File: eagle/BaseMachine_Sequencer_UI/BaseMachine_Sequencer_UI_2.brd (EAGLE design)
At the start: 71.7 x 46.6 mm, 4 parts, among them SW1 AK_TCTSW, SW2 AK_TCTSW

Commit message: Update: UI & UI2 Board Design
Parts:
- added JP2: PWR1, pinhead:1X02/90
- added JP3: PWR2, pinhead:1X02
- added JP4: PWR3, pinhead:1X02
- added JP5: PWR4, pinhead:1X02
- added JP6: PWR5, pinhead:1X02
- added SW3: AK_TCTSW, mylib2:TME1
- JP1: value (none) -> SW1
- moved JP1 15.5 mm to (39.1, 44.5)
- moved SW2 7.71 mm to (53.2, 15.2)
- moved RE1 5.75 mm to (10.2, 17.7)
- moved SW1 2.57 mm to (35.0, 15.6)
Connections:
- removed net N$3: JP1.1, RE1.P$2
- removed net N$6: JP1.4, SW2.3, SW2.4
- new net N$1: JP1.2, RE1.P$2
- new net N$2: JP1.5, SW2.3, SW2.4
- new net N$7: JP1.1, SW3.3, SW3.4
- new net VCC: JP2.1, JP3.1, JP4.1, JP5.1, JP6.1
- net GND: now also JP2.2, JP3.2, JP4.2, JP5.2, JP6.2, SW3.1, SW3.6; no longer JP1.5
- net N$4: now also JP1.3; no longer JP1.2
- net N$5: now also JP1.4; no longer JP1.3
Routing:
- net GND: track 0.00 -> 138.9 mm
- net N$1: track 0.00 -> 54.1 mm
- net N$4: track 0.00 -> 51.6 mm
- net N$2: track 0.00 -> 36.3 mm
- net N$5: track 0.00 -> 33.2 mm
- net N$7: track 0.00 -> 28.9 mm
- net VCC: track 0.00 -> 10.6 mm
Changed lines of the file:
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@@
 </autorouter>
 <elements>
-<element name="RE1" library="mylib2" package="RE_AK_DIP" value="RE_AK_DIP" x="12.73" y="22.86"/>
-<element name="SW1" library="mylib2" package="TME1" value="AK_TCTSW" x="32.44" y="15.6" rot="R90"/>
-<element name="SW2" library="mylib2" package="TME1" value="AK_TCTSW" x="60.96" y="15.24" rot="R90"/>
-<element name="JP1" library="pinhead" package="1X05/90" value="" x="54.55" y="45.72"/>
+<element name="RE1" library="mylib2" package="RE_AK_DIP" value="RE_AK_DIP" x="10.16" y="17.72"/>
+<element name="SW1" library="mylib2" package="TME1" value="AK_TCTSW" x="35.01" y="15.6" rot="R90"/>
+<element name="SW2" library="mylib2" package="TME1" value="AK_TCTSW" x="53.25" y="15.24" rot="R90"/>
+<element name="JP1" library="pinhead" package="1X05/90" value="SW1" x="39.13" y="44.45"/>
+<element name="SW3" library="mylib2" package="TME1" value="AK_TCTSW" x="10.25" y="36.77"/>
+<element name="JP2" library="pinhead" package="1X02/90" value="PWR1" x="63.44" y="44.42"/>
+<element name="JP3" library="pinhead" package="1X02" value="PWR2" x="63.44" y="37.92"/>
+<element name="JP4" library="pinhead" package="1X02" value="PWR3" x="63.44" y="35.29"/>
+<element name="JP5" library="pinhead" package="1X02" value="PWR4" x="63.44" y="32.66"/>
+<element name="JP6" library="pinhead" package="1X02" value="PWR5" x="63.44" y="30.03"/>
 </elements>
 <signals>
@@
 <contactref element="SW2" pad="1"/>
 <contactref element="RE1" pad="P$3"/>
-<contactref element="JP1" pad="5"/>
-<wire x1="57.15" y1="12.7" x2="59.63" y2="41.91" width="0" layer="19" extent="1-1"/>
-<wire x1="64.77" y1="12.7" x2="57.15" y2="12.7" width="0" layer="19" extent="1-1"/>
-<wire x1="36.25" y1="13.06" x2="57.15" y2="12.7" width="0" layer="19" extent="1-1"/>
-<wire x1="28.63" y1="13.06" x2="36.25" y2="13.06" width="0" layer="19" extent="1-1"/>
-<wire x1="12.73" y1="12.7" x2="28.63" y2="13.06" width="0" layer="19" extent="1-1"/>
-</signal>
-<signal name="N$3">
-<contactref element="RE1" pad="P$2"/>
-<contactref element="JP1" pad="1"/>
-<wire x1="10.19" y1="12.7" x2="49.47" y2="41.91" width="0" layer="19" extent="1-1"/>
+<contactref element="SW3" pad="1"/>
+<contactref element="SW3" pad="6"/>
+<contactref element="JP4" pad="2"/>
+<contactref element="JP5" pad="2"/>
+<contactref element="JP3" pad="2"/>
+<contactref element="JP6" pad="2"/>
+<contactref element="JP2" pad="2"/>
+<wire x1="7.71" y1="40.58" x2="7.71" y2="32.96" width="0.4064" layer="1"/>
+<wire x1="31.2" y1="13.06" x2="38.82" y2="13.06" width="0.4064" layer="1"/>
+<wire x1="49.44" y1="12.7" x2="56.54" y2="12.7" width="0.4064" layer="1"/>
+<wire x1="56.54" y1="12.7" x2="56.54" y2="12.85" width="0.4064" layer="1"/>
+<wire x1="56.54" y1="12.85" x2="57.06" y2="12.85" width="0.4064" layer="1"/>
+<wire x1="57.06" y1="12.85" x2="57.06" y2="12.7" width="0.4064" layer="1"/>
+<wire x1="64.71" y1="40.61" x2="64.71" y2="37.92" width="0.4064" layer="16"/>
+<wire x1="64.71" y1="37.92" x2="64.71" y2="35.29" width="0.4064" layer="16"/>
+<wire x1="64.71" y1="35.29" x2="64.71" y2="32.66" width="0.4064" layer="16"/>
+<wire x1="64.71" y1="32.66" x2="64.71" y2="30.03" width="0.4064" layer="16"/>
+<wire x1="64.71" y1="30.03" x2="64.25" y2="30.03" width="0.4064" layer="16"/>
+<wire x1="64.25" y1="30.03" x2="64.25" y2="12.85" width="0.4064" layer="16"/>
+<wire x1="64.25" y1="12.85" x2="57.06" y2="12.85" width="0.4064" layer="16"/>
+<wire x1="57.06" y1="12.85" x2="57.06" y2="12.7" width="0.4064" layer="16"/>
+<wire x1="49.44" y1="12.7" x2="38.82" y2="12.7" width="0.4064" layer="16"/>
+<wire x1="38.82" y1="12.7" x2="38.82" y2="13.06" width="0.4064" layer="16"/>
+<wire x1="31.2" y1="13.06" x2="30.84" y2="13.06" width="0.4064" layer="16"/>
+<wire x1="30.84" y1="13.06" x2="30.84" y2="5.14" width="0.4064" layer="16"/>
+<wire x1="30.84" y1="5.14" x2="10.28" y2="5.14" width="0.4064" layer="16"/>
+<wire x1="10.28" y1="5.14" x2="2.57" y2="5.14" width="0.4064" layer="16"/>
+<wire x1="2.57" y1="5.14" x2="2.57" y2="28.27" width="0.4064" layer="16"/>
+<wire x1="2.57" y1="28.27" x2="3.02" y2="28.27" width="0.4064" layer="16"/>
+<wire x1="3.02" y1="28.27" x2="7.71" y2="32.96" width="0.4064" layer="16"/>
+<wire x1="10.16" y1="7.56" x2="10.16" y2="5.26" width="0.4064" layer="16"/>
+<wire x1="10.16" y1="5.26" x2="10.28" y2="5.14" width="0.4064" layer="16"/>
 </signal>
 <signal name="N$4">
 <contactref element="RE1" pad="P$4"/>
-<contactref element="JP1" pad="2"/>
-<wire x1="15.27" y1="12.7" x2="52.01" y2="41.91" width="0" layer="19" extent="1-1"/>
+<contactref element="JP1" pad="3"/>
+<wire x1="12.7" y1="7.56" x2="12.7" y2="17.84" width="0.4064" layer="16"/>
+<wire x1="12.7" y1="17.84" x2="12.85" y2="17.99" width="0.4064" layer="16"/>
+<wire x1="12.85" y1="17.99" x2="12.85" y2="20.56" width="0.4064" layer="16"/>
+<wire x1="12.85" y1="20.56" x2="25.7" y2="20.56" width="0.4064" layer="16"/>
+<wire x1="25.7" y1="20.56" x2="38.55" y2="33.41" width="0.4064" layer="16"/>
+<wire x1="38.55" y1="33.41" x2="38.55" y2="40.06" width="0.4064" layer="16"/>
+<wire x1="38.55" y1="40.06" x2="39.13" y2="40.64" width="0.4064" layer="16"/>
 </signal>
 <signal name="N$5">
 <contactref element="SW1" pad="4"/>
 <contactref element="SW1" pad="3"/>
-<contactref element="JP1" pad="3"/>
-<wire x1="36.25" y1="18.14" x2="54.55" y2="41.91" width="0" layer="19" extent="1-1"/>
-<wire x1="28.63" y1="18.14" x2="36.25" y2="18.14" width="0" layer="19" extent="1-1"/>
+<contactref element="JP1" pad="4"/>
+<wire x1="31.2" y1="18.14" x2="38.55" y2="18.14" width="0.4064" layer="1"/>
+<wire x1="38.55" y1="18.14" x2="38.55" y2="17.99" width="0.4064" layer="1"/>
+<wire x1="38.55" y1="17.99" x2="38.82" y2="17.99" width="0.4064" layer="1"/>
+<wire x1="38.82" y1="17.99" x2="38.82" y2="18.14" width="0.4064" layer="1"/>
+<wire x1="38.82" y1="18.14" x2="40.97" y2="18.14" width="0.4064" layer="16"/>
+<wire x1="40.97" y1="18.14" x2="41.12" y2="17.99" width="0.4064" layer="16"/>
+<wire x1="41.12" y1="17.99" x2="41.12" y2="40.09" width="0.4064" layer="16"/>
+<wire x1="41.12" y1="40.09" x2="41.67" y2="40.64" width="0.4064" layer="16"/>
 </signal>
-<signal name="N$6">
+<signal name="N$2">
 <contactref element="SW2" pad="4"/>
 <contactref element="SW2" pad="3"/>
-<contactref element="JP1" pad="4"/>
-<wire x1="57.15" y1="17.78" x2="57.09" y2="41.91" width="0" layer="19" extent="1-1"/>
-<wire x1="64.77" y1="17.78" x2="57.15" y2="17.78" width="0" layer="19" extent="1-1"/>
+<contactref element="JP1" pad="5"/>
+<wire x1="49.44" y1="17.78" x2="57.06" y2="17.78" width="0.4064" layer="1"/>
+<wire x1="49.44" y1="17.78" x2="43.9" y2="17.78" width="0.4064" layer="16"/>
+<wire x1="43.9" y1="17.78" x2="43.69" y2="17.99" width="0.4064" layer="16"/>
+<wire x1="43.69" y1="17.99" x2="43.69" y2="40.12" width="0.4064" layer="16"/>
+<wire x1="43.69" y1="40.12" x2="44.21" y2="40.64" width="0.4064" layer="16"/>
+</signal>
+<signal name="N$7">
+<contactref element="SW3" pad="4"/>
+<contactref element="SW3" pad="3"/>
+<contactref element="JP1" pad="1"/>
+<wire x1="12.79" y1="40.58" x2="12.79" y2="32.96" width="0.4064" layer="1"/>
+<wire x1="12.79" y1="40.58" x2="33.99" y2="40.58" width="0.4064" layer="16"/>
+<wire x1="33.99" y1="40.58" x2="34.05" y2="40.64" width="0.4064" layer="16"/>
+</signal>
+<signal name="N$1">
+<contactref element="RE1" pad="P$2"/>
+<contactref element="JP1" pad="2"/>
+<wire x1="7.62" y1="7.56" x2="7.62" y2="23.04" width="0.4064" layer="16"/>
+<wire x1="7.62" y1="23.04" x2="7.71" y2="23.13" width="0.4064" layer="16"/>
+<wire x1="7.71" y1="23.13" x2="23.13" y2="23.13" width="0.4064" layer="16"/>
+<wire x1="23.13" y1="23.13" x2="35.98" y2="35.98" width="0.4064" layer="16"/>
+<wire x1="35.98" y1="35.98" x2="35.98" y2="40.03" width="0.4064" layer="16"/>
+<wire x1="35.98" y1="40.03" x2="36.59" y2="40.64" width="0.4064" layer="16"/>
+</signal>
+<signal name="VCC">
+<contactref element="JP6" pad="1"/>
+<contactref element="JP3" pad="1"/>
+<contactref element="JP5" pad="1"/>
+<contactref element="JP4" pad="1"/>
+<contactref element="JP2" pad="1"/>
+<wire x1="62.17" y1="40.61" x2="62.17" y2="37.92" width="0.4064" layer="16"/>
+<wire x1="62.17" y1="37.92" x2="62.17" y2="35.29" width="0.4064" layer="16"/>
+<wire x1="62.17" y1="35.29" x2="62.17" y2="32.66" width="0.4064" layer="16"/>
+<wire x1="62.17" y1="32.66" x2="62.17" y2="30.03" width="0.4064" layer="16"/>
 </signal>
 </signals>

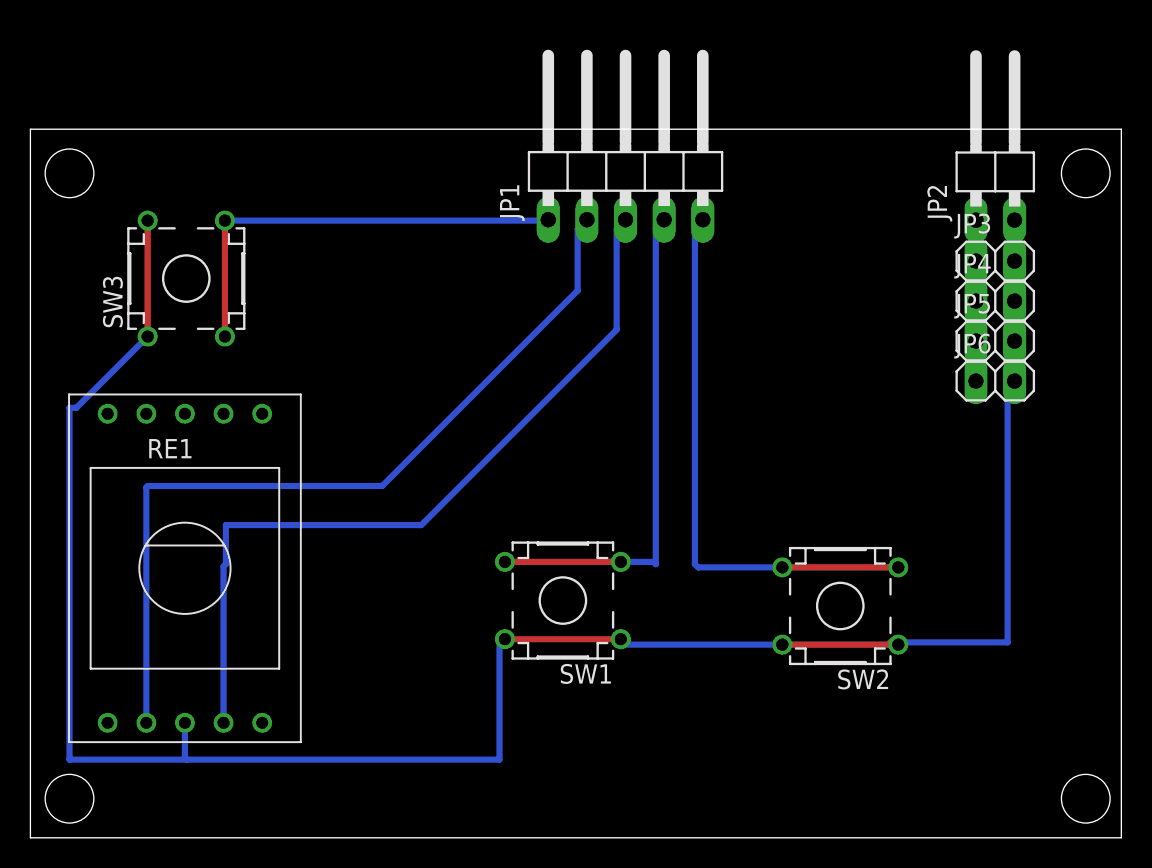
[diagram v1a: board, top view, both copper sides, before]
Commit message: Add: Nucleo firmware's binaries
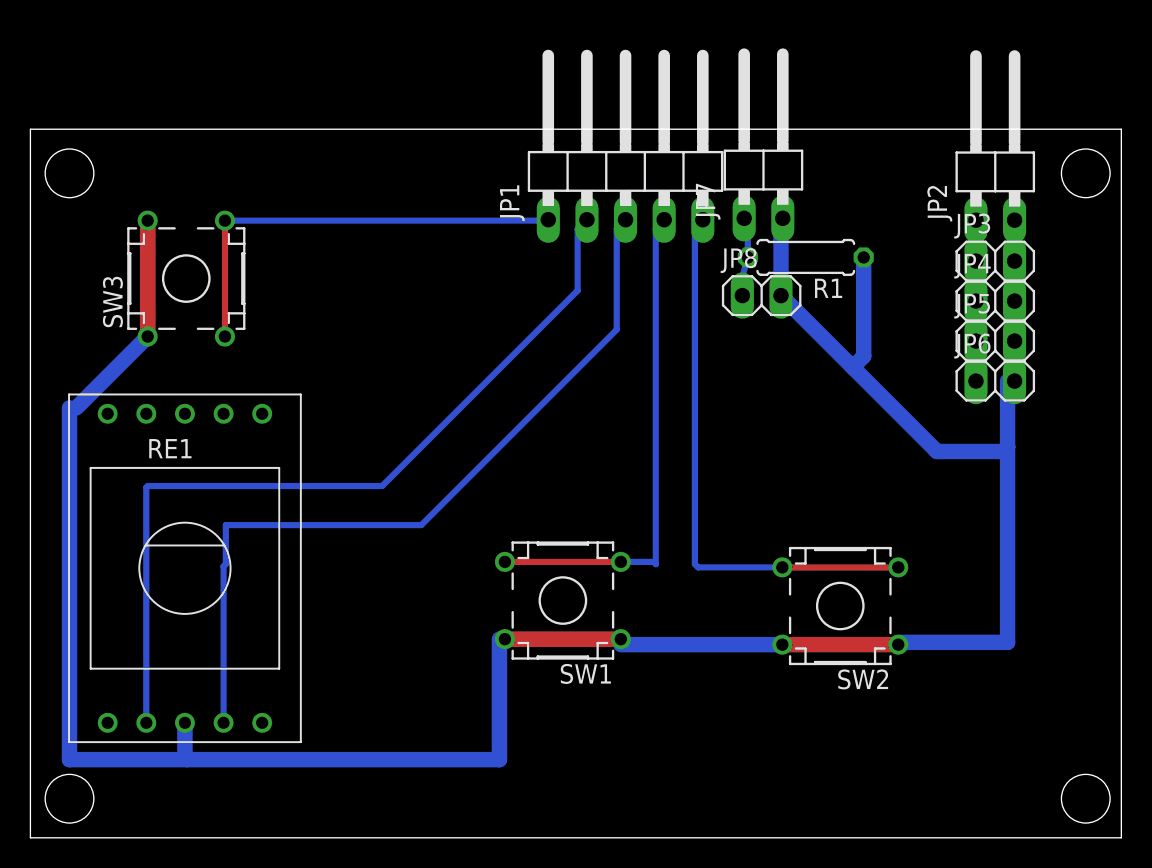
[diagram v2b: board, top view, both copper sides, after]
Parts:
- added JP7: SYNC, pinhead:1X02/90
- added JP8: SYNC, pinhead:1X02
- added R1: 4.7k, rcl:0207/7
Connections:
- new net N$6: JP7.1, JP8.1, R1.2
- net GND: now also JP7.2, JP8.2, R1.1
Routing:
- net GND: track 138.9 -> 170.9 mm
- net N$6: track 0.00 -> 5.37 mm
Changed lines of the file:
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@@
 <element name="JP5" library="pinhead" package="1X02" value="PWR4" x="63.44" y="32.66"/>
 <element name="JP6" library="pinhead" package="1X02" value="PWR5" x="63.44" y="30.03"/>
+<element name="JP7" library="pinhead" package="1X02/90" value="SYNC" x="48.2" y="44.54"/>
+<element name="JP8" library="pinhead" package="1X02" value="SYNC" x="48.08" y="35.65"/>
+<element name="R1" library="rcl" package="0207/7" value="4.7k" x="50.98" y="38.16" rot="R180"/>
 </elements>
 <signals>
@@
 <contactref element="JP6" pad="2"/>
 <contactref element="JP2" pad="2"/>
-<wire x1="7.71" y1="40.58" x2="7.71" y2="32.96" width="0.4064" layer="1"/>
-<wire x1="31.2" y1="13.06" x2="38.82" y2="13.06" width="0.4064" layer="1"/>
-<wire x1="49.44" y1="12.7" x2="56.54" y2="12.7" width="0.4064" layer="1"/>
+<wire x1="7.71" y1="40.58" x2="7.71" y2="32.96" width="1.016" layer="1"/>
+<wire x1="31.2" y1="13.06" x2="38.82" y2="13.06" width="1.016" layer="1"/>
+<wire x1="49.44" y1="12.7" x2="56.54" y2="12.7" width="1.016" layer="1"/>
 <wire x1="56.54" y1="12.7" x2="56.54" y2="12.85" width="0.4064" layer="1"/>
 <wire x1="56.54" y1="12.85" x2="57.06" y2="12.85" width="0.4064" layer="1"/>
 <wire x1="57.06" y1="12.85" x2="57.06" y2="12.7" width="0.4064" layer="1"/>
-<wire x1="64.71" y1="40.61" x2="64.71" y2="37.92" width="0.4064" layer="16"/>
-<wire x1="64.71" y1="37.92" x2="64.71" y2="35.29" width="0.4064" layer="16"/>
-<wire x1="64.71" y1="35.29" x2="64.71" y2="32.66" width="0.4064" layer="16"/>
-<wire x1="64.71" y1="32.66" x2="64.71" y2="30.03" width="0.4064" layer="16"/>
+<wire x1="64.71" y1="40.61" x2="64.71" y2="37.92" width="1.016" layer="16"/>
+<wire x1="64.71" y1="37.92" x2="64.71" y2="35.29" width="1.016" layer="16"/>
+<wire x1="64.71" y1="35.29" x2="64.71" y2="32.66" width="1.016" layer="16"/>
+<wire x1="64.71" y1="32.66" x2="64.71" y2="30.03" width="1.016" layer="16"/>
 <wire x1="64.71" y1="30.03" x2="64.25" y2="30.03" width="0.4064" layer="16"/>
-<wire x1="64.25" y1="30.03" x2="64.25" y2="12.85" width="0.4064" layer="16"/>
-<wire x1="64.25" y1="12.85" x2="57.06" y2="12.85" width="0.4064" layer="16"/>
+<wire x1="64.25" y1="30.03" x2="64.25" y2="25.7" width="1.016" layer="16"/>
+<wire x1="64.25" y1="25.7" x2="64.25" y2="12.85" width="1.016" layer="16"/>
+<wire x1="64.25" y1="12.85" x2="57.06" y2="12.85" width="1.016" layer="16"/>
 <wire x1="57.06" y1="12.85" x2="57.06" y2="12.7" width="0.4064" layer="16"/>
-<wire x1="49.44" y1="12.7" x2="38.82" y2="12.7" width="0.4064" layer="16"/>
+<wire x1="49.44" y1="12.7" x2="38.82" y2="12.7" width="1.016" layer="16"/>
 <wire x1="38.82" y1="12.7" x2="38.82" y2="13.06" width="0.4064" layer="16"/>
 <wire x1="31.2" y1="13.06" x2="30.84" y2="13.06" width="0.4064" layer="16"/>
-<wire x1="30.84" y1="13.06" x2="30.84" y2="5.14" width="0.4064" layer="16"/>
-<wire x1="30.84" y1="5.14" x2="10.28" y2="5.14" width="0.4064" layer="16"/>
-<wire x1="10.28" y1="5.14" x2="2.57" y2="5.14" width="0.4064" layer="16"/>
-<wire x1="2.57" y1="5.14" x2="2.57" y2="28.27" width="0.4064" layer="16"/>
+<wire x1="30.84" y1="13.06" x2="30.84" y2="5.14" width="1.016" layer="16"/>
+<wire x1="30.84" y1="5.14" x2="10.28" y2="5.14" width="1.016" layer="16"/>
+<wire x1="10.28" y1="5.14" x2="2.57" y2="5.14" width="1.016" layer="16"/>
+<wire x1="2.57" y1="5.14" x2="2.57" y2="28.27" width="1.016" layer="16"/>
 <wire x1="2.57" y1="28.27" x2="3.02" y2="28.27" width="0.4064" layer="16"/>
-<wire x1="3.02" y1="28.27" x2="7.71" y2="32.96" width="0.4064" layer="16"/>
-<wire x1="10.16" y1="7.56" x2="10.16" y2="5.26" width="0.4064" layer="16"/>
+<wire x1="3.02" y1="28.27" x2="7.71" y2="32.96" width="1.016" layer="16"/>
+<wire x1="10.16" y1="7.56" x2="10.16" y2="5.26" width="1.016" layer="16"/>
 <wire x1="10.16" y1="5.26" x2="10.28" y2="5.14" width="0.4064" layer="16"/>
+<contactref element="R1" pad="1"/>
+<contactref element="JP8" pad="2"/>
+<contactref element="JP7" pad="2"/>
+<wire x1="49.47" y1="40.73" x2="49.35" y2="40.73" width="0.4064" layer="16"/>
+<wire x1="49.35" y1="40.73" x2="49.35" y2="35.65" width="1.016" layer="16"/>
+<wire x1="59.6" y1="25.4" x2="63.95" y2="25.4" width="1.016" layer="16"/>
+<wire x1="63.95" y1="25.4" x2="64.25" y2="25.7" width="1.016" layer="16"/>
+<wire x1="59.6" y1="25.4" x2="54.065" y2="30.935" width="1.016" layer="16"/>
+<wire x1="54.065" y1="30.935" x2="49.35" y2="35.65" width="1.016" layer="16"/>
+<wire x1="54.79" y1="38.16" x2="54.79" y2="31.66" width="1.016" layer="16"/>
+<wire x1="54.79" y1="31.66" x2="54.065" y2="30.935" width="1.016" layer="16"/>
 </signal>
 <signal name="N$4">
@@
 <wire x1="62.17" y1="32.66" x2="62.17" y2="30.03" width="0.4064" layer="16"/>
 </signal>
+<signal name="N$6">
+<contactref element="R1" pad="2"/>
+<contactref element="JP7" pad="1"/>
+<contactref element="JP8" pad="1"/>
+<wire x1="46.93" y1="40.73" x2="47.17" y2="40.73" width="0.4064" layer="16"/>
+<wire x1="47.17" y1="40.73" x2="47.17" y2="38.16" width="0.4064" layer="16"/>
+<wire x1="47.17" y1="38.16" x2="46.81" y2="36.89" width="0.4064" layer="16"/>
+<wire x1="46.81" y1="36.89" x2="46.81" y2="35.65" width="0.4064" layer="16"/>
+</signal>
 </signals>
+<errors>
+</errors>
 </board>
 </drawing>
